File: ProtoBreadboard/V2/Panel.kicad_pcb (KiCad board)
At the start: 2 copper layers, 121.8 x 172.4 mm, 255 parts, among them IC1 AT90USB1286-AU, IC2 BSS138, IC3 BSS138, IC4 BSS138, IC5 BSS138, J1 Conn_01x30_Female, J10 Conn_01x04_Female, J11 Conn_01x32_Female, J12 Conn_01x06_Female, J13 Conn_01x08_Female, J14 Conn_01x08_Female, J15 Conn_01x04_Female, J16 Conn_01x03_Female, J17 Conn_01x03_Female, J18 Conn_01x07_Female, J19 Conn_01x02_Female, J2 Conn_01x10_Female, J20 Conn_01x02_Female, J21 Conn_01x02_Female, J22 AVR-ISP-6, J23 Conn_01x02_Female, J24 Conn_01x03_Female, J25 Conn_01x07_Female, J26 Conn_01x03_Female, J27 Conn_02x03_Counter_Clockwise, J28 Conn_01x03_Female, J29 Conn_01x02_Female, J3 Conn_01x32_Female, J30 Conn_01x02_Female, J31 Conn_01x02_Female, J32 Conn_01x02_Female, J33 Conn_01x10_Female, J34 Conn_01x10_Female, J35 Conn_01x10_Female, J36 Conn_01x10_Female, J37 Conn_01x10_Female, J38 Conn_01x10_Female, J39 Conn_01x10_Female, J4 Conn_01x10_Female, J40 Conn_01x10_Female, J41 Conn_01x10_Female, J42 Conn_01x10_Female, J43 Conn_01x10_Female, J44 Conn_01x10_Female, J45 Conn_01x10_Female, J46 Conn_01x10_Female, J47 Conn_01x10_Female, J48 Conn_01x10_Female, J49 Conn_01x10_Female, J5 Conn_01x30_Female, J50 Conn_01x10_Female, J51 Conn_01x03_Female, J52 Conn_01x02_Female, J53 Conn_01x04_Female, J54 Conn_01x02_Female, J55 Conn_01x02_Female, J56 Conn_01x02_Female, J57 Conn_01x02_Female, J58 Conn_01x02_Female, J6 Conn_01x02_Female, J7 Conn_01x02_Female, J8 Conn_01x06_Female, J9 Conn_01x04_Female, SW1 RotaryEncoder_Switch, SW2 RotaryEncoder_Switch, U1 IS31FL3741A, U2 AP2112K-3.3, U3 PRTR5V0U2X, U4 AP2112K-3.3, Y1 Crystal, Y2 Crystal, Y3 Crystal

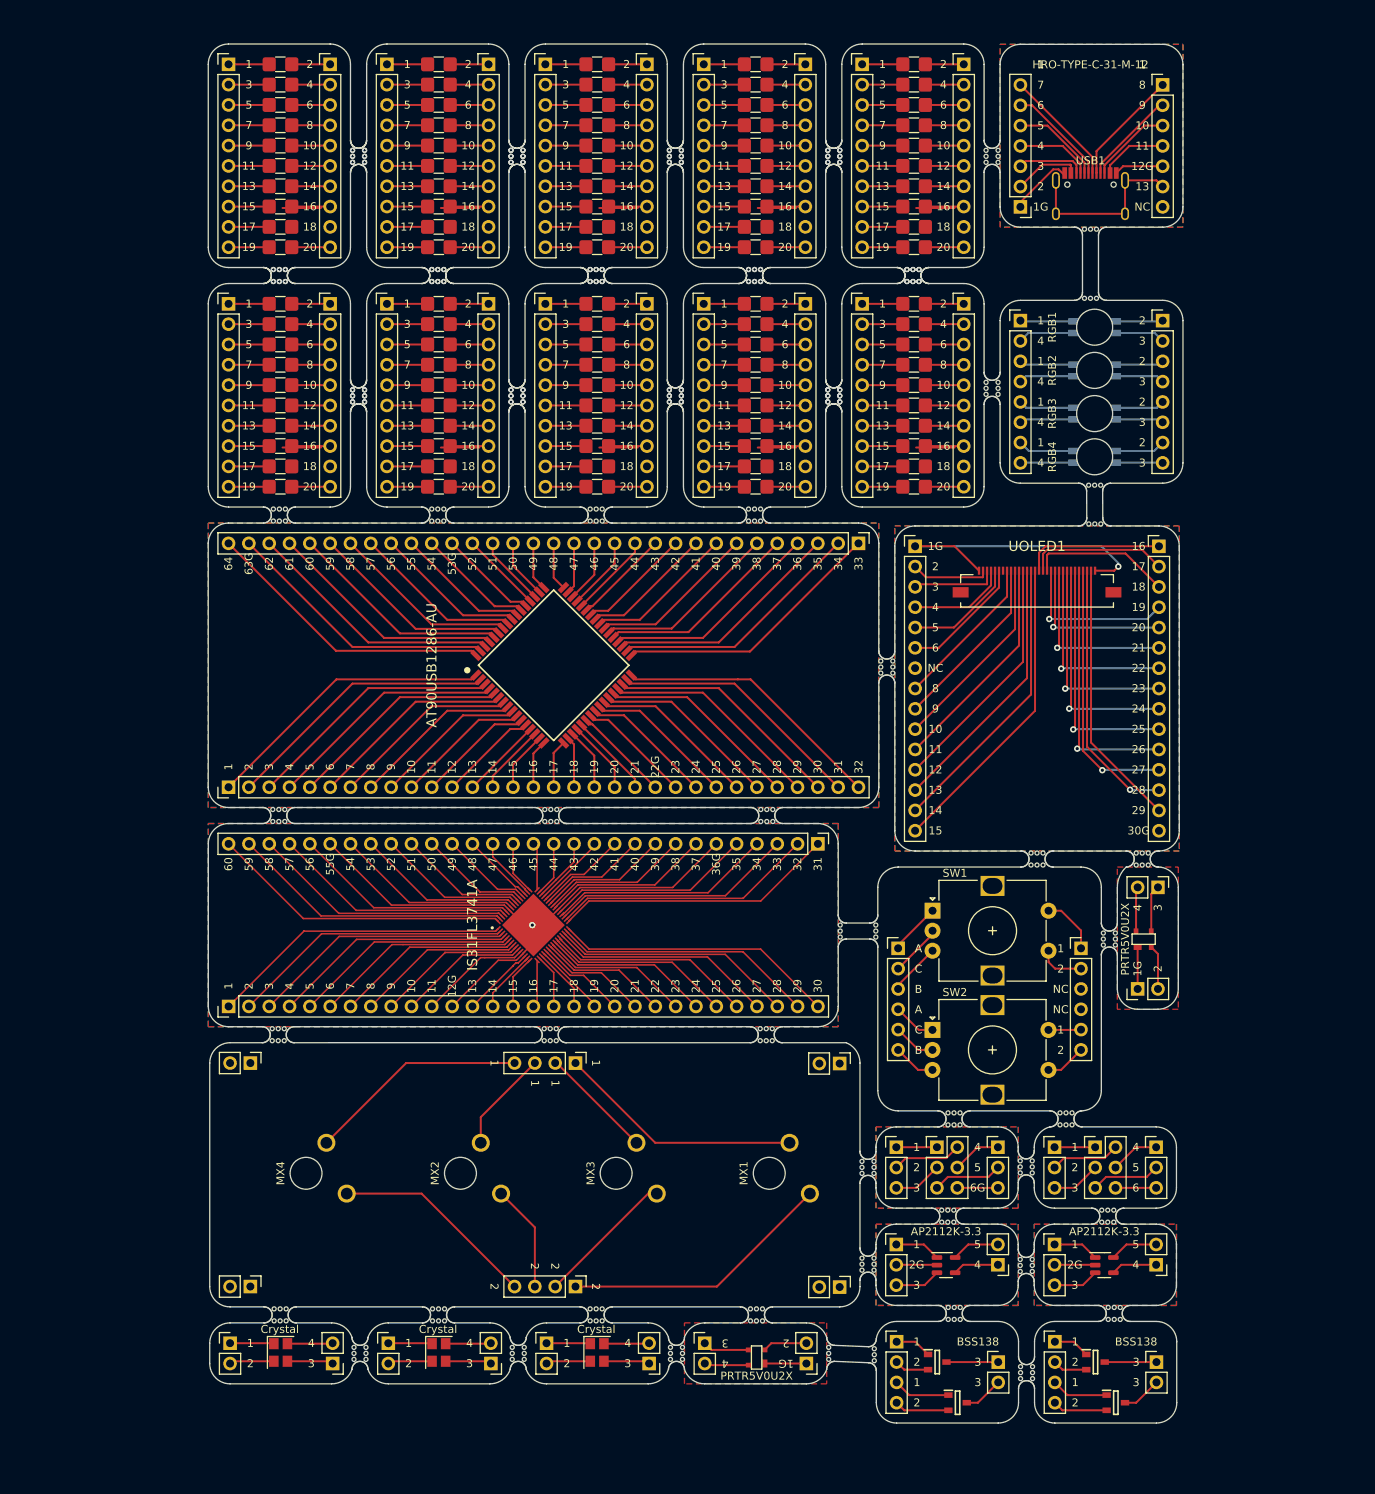
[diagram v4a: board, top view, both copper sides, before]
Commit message: Small alignment error for the crystal in the panel
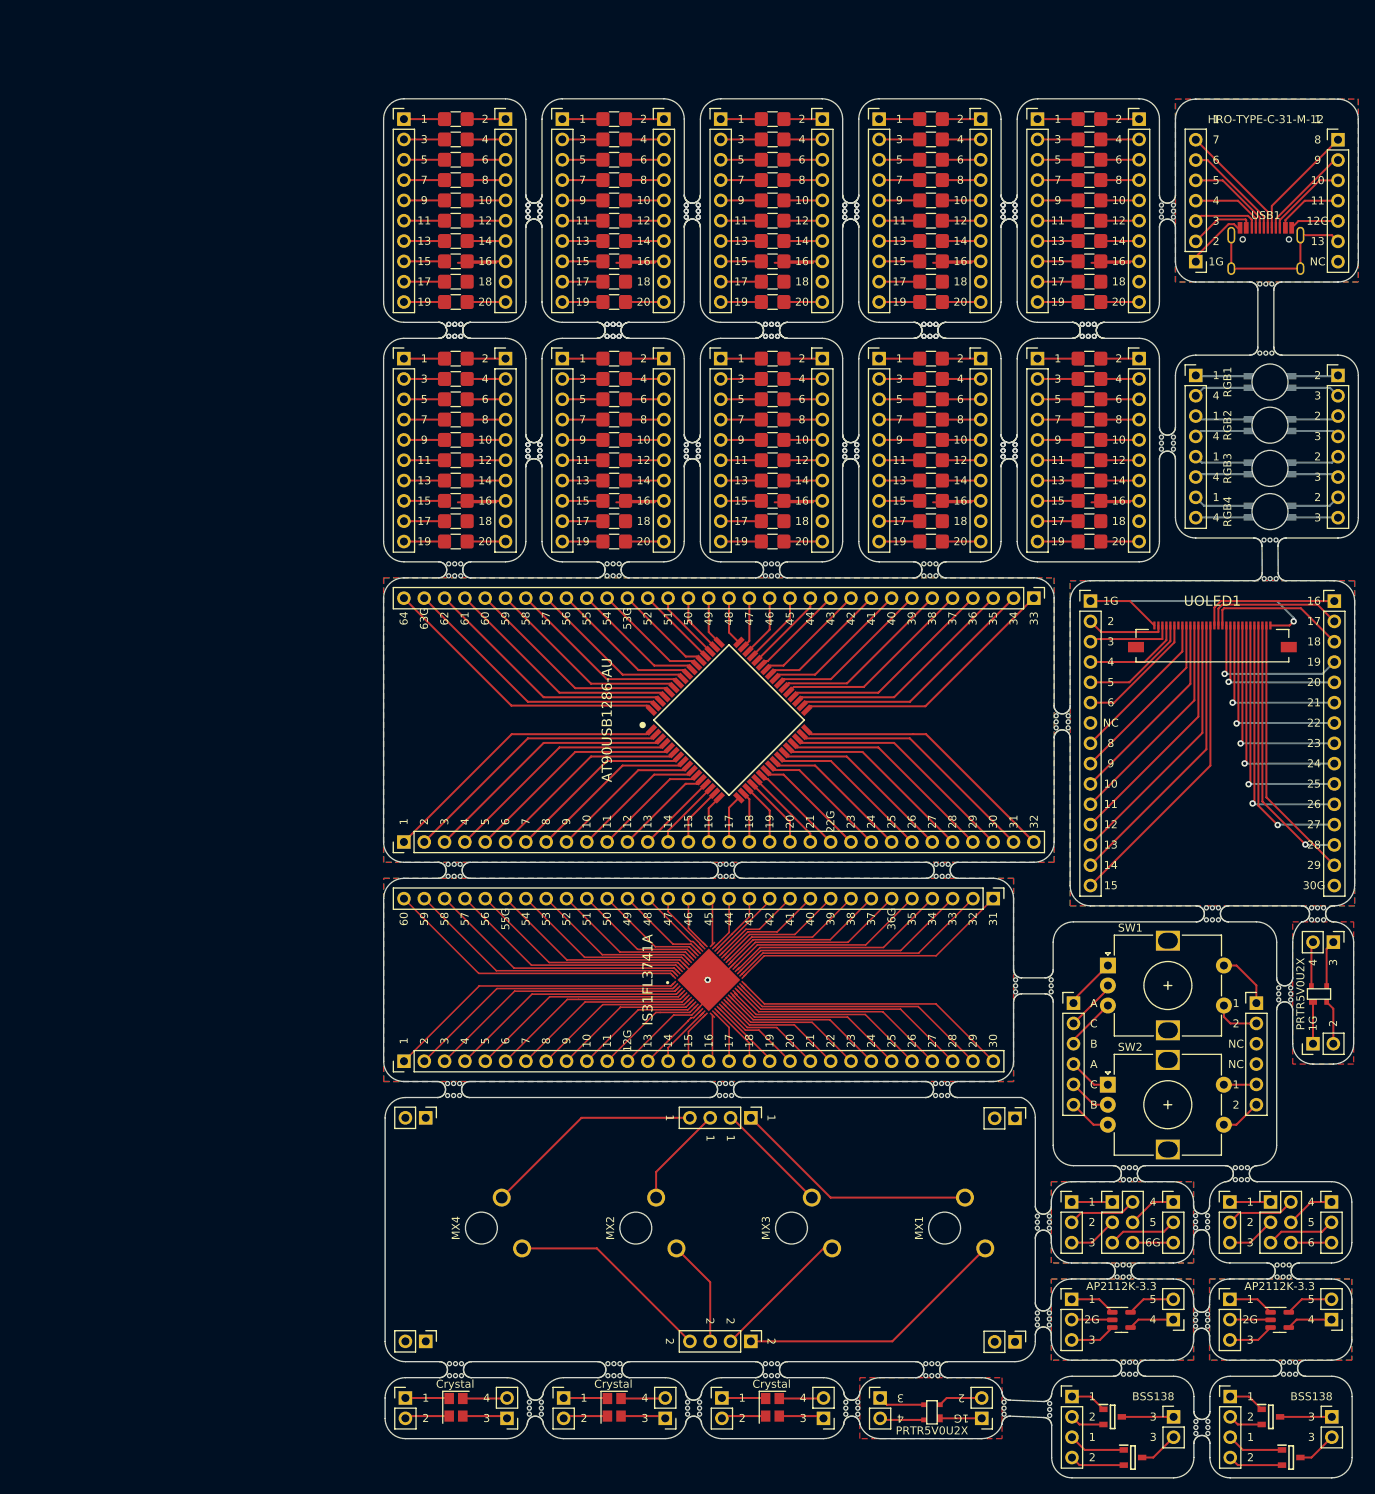
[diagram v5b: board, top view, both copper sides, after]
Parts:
- moved J26 23.0 mm to (168.2, 171.1)
- moved UOLED1 23.0 mm to (166.0, 101.0)
- moved mouse-bite-2mm-slot 23.0 mm to (132.2, 129.6)
- moved mouse-bite-2mm-slot 23.0 mm to (173.2, 92.4)
- moved mouse-bite-2mm-slot 23.0 mm to (147.2, 111.1)
- moved IC3 23.0 mm to (156.1, 203.0)
- moved IC5 23.0 mm to (175.8, 203.0)
- moved J12 23.0 mm to (171.5, 146.2)
- moved J51 23.0 mm to (168.2, 183.2)
- moved MX1 23.0 mm to (132.5, 174.3)
- moved SW1 23.0 mm to (152.9, 141.5)
- moved U2 23.0 mm to (154.6, 185.8)
- moved U4 23.0 mm to (174.4, 185.8)
- moved mouse-bite-2mm-slot 23.0 mm to (166.0, 135.1)
- moved mouse-bite-2mm-slot 23.0 mm to (175.0, 145.1)
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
